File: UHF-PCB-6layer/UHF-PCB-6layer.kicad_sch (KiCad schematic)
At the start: 14 parts, among them IC1 MC100EL1648DG, U1 MAC-24+, U3 TAV1-331+, U4 TPS3103K33DBVR, U5 XMSM0G3507SPT, U6 XC7A100T-CSG324_A

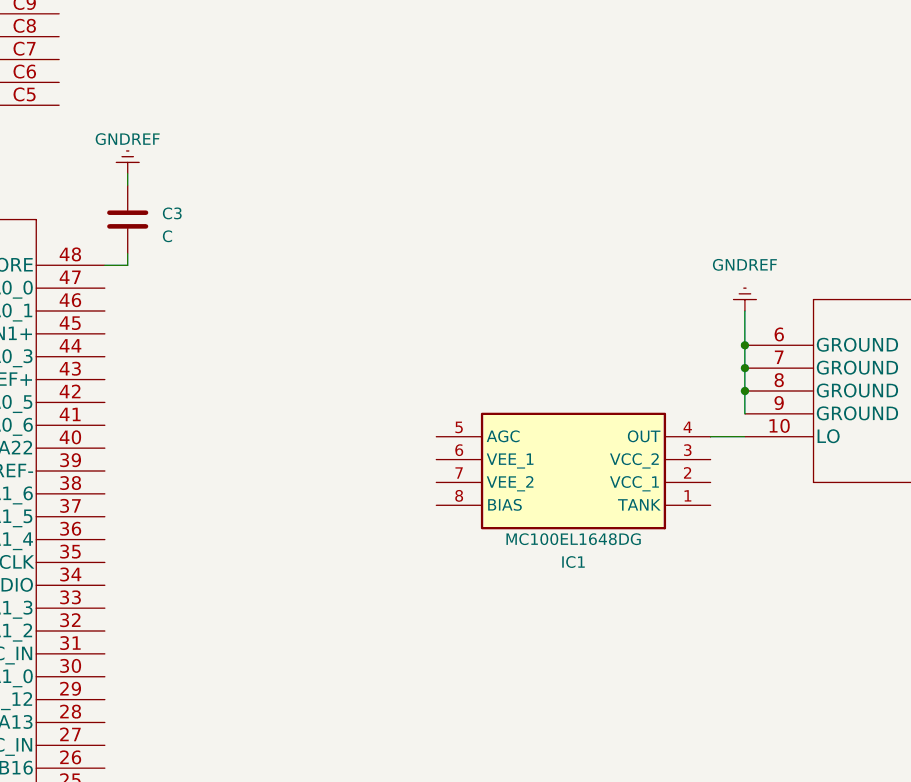
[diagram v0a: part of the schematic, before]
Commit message: added more to VCO circuit
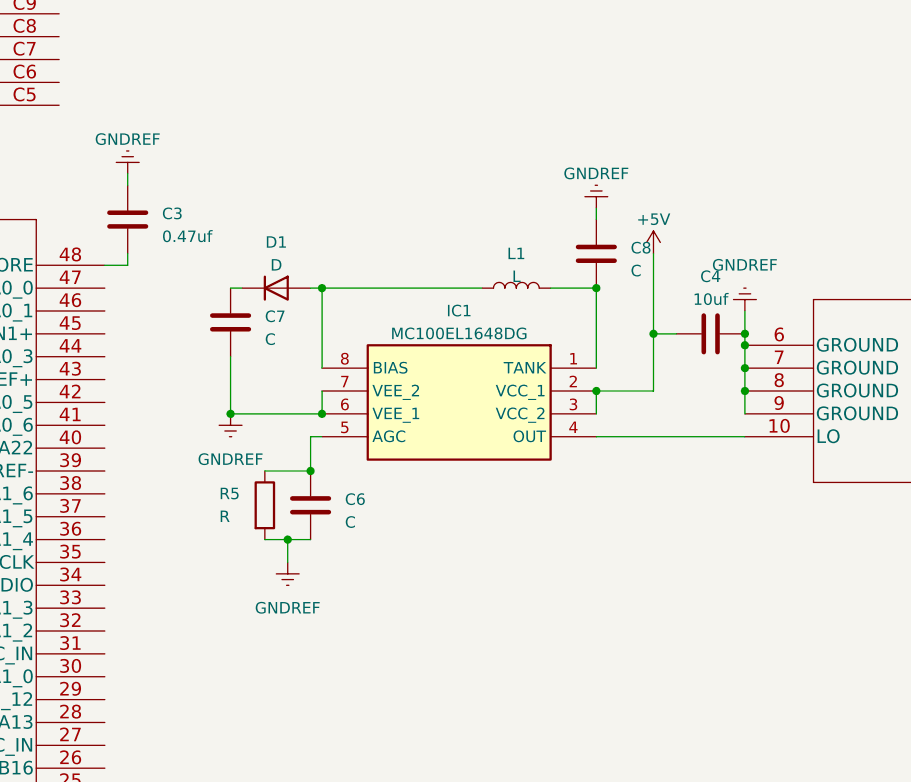
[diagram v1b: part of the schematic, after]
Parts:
- added C4: 10uf, Capacitor_SMD:C_0603_1608Metric, symbol Device:C
- added C6, C7, C8: C, Capacitor_SMD:C_0603_1608Metric, symbol Device:C
- added D1: D, Diode_SMD:D_0603_1608Metric, symbol Device:D
- added L1: L, Inductor_SMD:L_0603_1608Metric, symbol Device:L
- added R5: R, Resistor_SMD:R_0603_1608Metric, symbol Device:R
- C3: value C -> 0.47uf
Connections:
- net +5V: now also IC1.2 (VCC_1), IC1.3 (VCC_2), C4.2
- net GNDREF: now also IC1.6 (VEE_1), IC1.7 (VEE_2), C4.1, C6.1, C7.2, C8.2, R5.2
- net at IC1.1 (TANK): now also C8.1, L1.2
- net at IC1.5 (AGC): now also C6.2, R5.1
- net at IC1.8 (BIAS): now also D1.2 (A), L1.1
- new net: C7.1, D1.1 (K)
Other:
- moved on the sheet: IC1

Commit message: added some gnds
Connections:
- net GNDREF: now also U3.1 (GND)
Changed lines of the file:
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@@
+    (stroke (width 0) (type default))
+  )
+  (wire (pts (xy 373.38 129.54) (xy 373.38 134.62))
     (stroke (width 0) (type default))
   )
@@
         )
       )
+    )
+  )
+  (symbol (lib_id "power:GNDREF") (at 373.38 129.54 180) (unit 1)
+    (in_bom yes) (on_board yes) (dnp no) (fields_autoplaced)
+    (property "Reference" "#PWR013" (at 373.38 123.19 0)
+      (effects (font (size 1.27 1.27)) hide)
+    )
+    (property "Value" "GNDREF" (at 373.38 125.73 0)
+      (effects (font (size 1.27 1.27)))
+    )
+    (property "Footprint" "" (at 373.38 129.54 0)
+      (effects (font (size 1.27 1.27)) hide)
+    )
+    (property "Datasheet" "" (at 373.38 129.54 0)
+      (effects (font (size 1.27 1.27)) hide)
+    )
+    (pin "1")
+    (instances
+      (project "UHF-PCB-6layer"
+        (path "/408f5dbf-8c57-4b84-b0cc-1d788fcf6d08"
+          (reference "#PWR013") (unit 1)
+        )
+      )

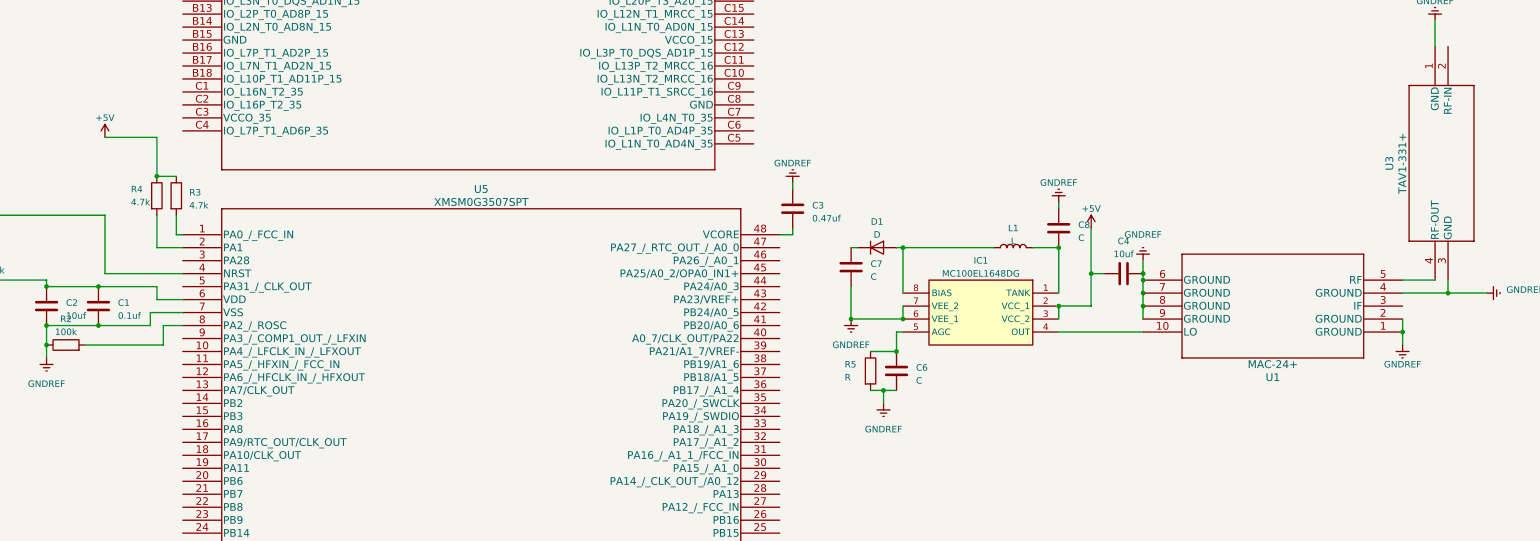
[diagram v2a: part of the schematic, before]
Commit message: added connections between FPGA and micro
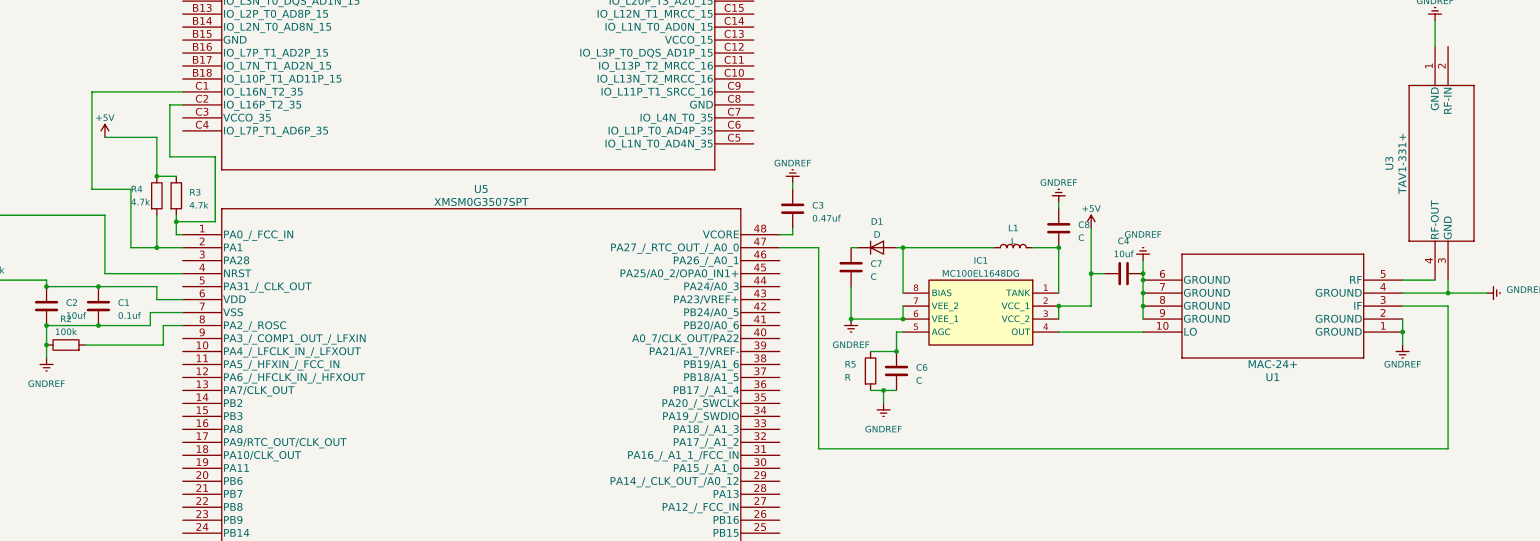
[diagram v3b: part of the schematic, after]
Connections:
- net at U1.3 (IF): now also U5.47 (PA27_/_RTC_OUT_/_A0_0)
- net at R3.2, U5.1 (PA0_/_FCC_IN): now also U6.C2 (IO_L16P_T2_35)
- net at R4.2, U5.2 (PA1): now also U6.C1 (IO_L16N_T2_35)
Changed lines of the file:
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@@
     (rev "MK1")
   )
+  (junction (at 127 168.91) (diameter 0) (color 0 0 0 0)
+  )
   (junction (at 306.07 179.07) (diameter 0) (color 0 0 0 0)
   )
@@
   (junction (at 299.72 185.42) (diameter 0) (color 0 0 0 0)
   )
+  (junction (at 123.19 173.99) (diameter 0) (color 0 0 0 0)
+  )
   (junction (at 123.19 160.02) (diameter 0) (color 0 0 0 0)
   )
@@
     (stroke (width 0) (type default))
   )
+  (wire (pts (xy 375.92 185.42) (xy 367.03 185.42))
+    (stroke (width 0) (type default))
+  )
   (wire (pts (xy 128.27 186.69) (xy 121.92 186.69))
     (stroke (width 0) (type default))
@@
     (stroke (width 0) (type default))
   )
+  (wire (pts (xy 128.27 143.51) (xy 110.49 143.51))
+    (stroke (width 0) (type default))
+  )
   (wire (pts (xy 306.07 170.18) (xy 306.07 179.07))
     (stroke (width 0) (type default))
@@
     (stroke (width 0) (type default))
   )
+  (wire (pts (xy 127 168.91) (xy 127 167.64))
+    (stroke (width 0) (type default))
+  )
   (wire (pts (xy 316.23 182.88) (xy 316.23 180.34))
     (stroke (width 0) (type default))
   )
+  (wire (pts (xy 252.73 213.36) (xy 375.92 213.36))
+    (stroke (width 0) (type default))
+  )
   (wire (pts (xy 375.92 182.88) (xy 367.03 182.88))
     (stroke (width 0) (type default))
   )
+  (wire (pts (xy 125.73 156.21) (xy 134.62 156.21))
+    (stroke (width 0) (type default))
+  )
   (wire (pts (xy 121.92 189.23) (xy 111.76 189.23))
     (stroke (width 0) (type default))
@@
     (stroke (width 0) (type default))
   )
+  (wire (pts (xy 110.49 143.51) (xy 110.49 162.56))
+    (stroke (width 0) (type default))
+  )
   (wire (pts (xy 316.23 185.42) (xy 316.23 182.88))
     (stroke (width 0) (type default))
@@
     (stroke (width 0) (type default))
   )
-  (wire (pts (xy 127 171.45) (xy 127 167.64))
+  (wire (pts (xy 127 171.45) (xy 127 168.91))
     (stroke (width 0) (type default))
   )
@@
     (stroke (width 0) (type default))
   )
+  (wire (pts (xy 110.49 162.56) (xy 118.11 162.56))
+    (stroke (width 0) (type default))
+  )
   (wire (pts (xy 247.65 171.45) (xy 245.11 171.45))
     (stroke (width 0) (type default))
@@
     (stroke (width 0) (type default))
   )
+  (wire (pts (xy 134.62 168.91) (xy 127 168.91))
+    (stroke (width 0) (type default))
+  )
   (wire (pts (xy 316.23 180.34) (xy 316.23 179.07))
     (stroke (width 0) (type default))
@@
     (stroke (width 0) (type default))
   )
+  (wire (pts (xy 128.27 146.05) (xy 125.73 146.05))
+    (stroke (width 0) (type default))
+  )
   (wire (pts (xy 247.65 161.29) (xy 247.65 162.56))
     (stroke (width 0) (type default))
@@
     (stroke (width 0) (type default))
   )
+  (wire (pts (xy 252.73 173.99) (xy 252.73 213.36))
+    (stroke (width 0) (type default))
+  )
   (wire (pts (xy 267.97 190.5) (xy 267.97 194.31))
     (stroke (width 0) (type default))
@@
     (stroke (width 0) (type default))
   )
+  (wire (pts (xy 118.11 173.99) (xy 123.19 173.99))
+    (stroke (width 0) (type default))
+  )
   (wire (pts (xy 259.08 181.61) (xy 259.08 187.96))
     (stroke (width 0) (type default))
@@
     (stroke (width 0) (type default))
   )
+  (wire (pts (xy 134.62 156.21) (xy 134.62 168.91))
+    (stroke (width 0) (type default))
+  )
   (wire (pts (xy 123.19 173.99) (xy 123.19 167.64))
     (stroke (width 0) (type default))
   )
+  (wire (pts (xy 118.11 162.56) (xy 118.11 173.99))
+    (stroke (width 0) (type default))
+  )
   (wire (pts (xy 128.27 189.23) (xy 124.46 189.23))
     (stroke (width 0) (type default))
@@
     (stroke (width 0) (type default))
   )
+  (wire (pts (xy 375.92 213.36) (xy 375.92 185.42))
+    (stroke (width 0) (type default))
+  )
   (wire (pts (xy 265.43 201.93) (xy 265.43 204.47))
     (stroke (width 0) (type default))
@@
     (stroke (width 0) (type default))
   )
+  (wire (pts (xy 245.11 173.99) (xy 252.73 173.99))
+    (stroke (width 0) (type default))
+  )
   (wire (pts (xy 294.64 173.99) (xy 299.72 173.99))
     (stroke (width 0) (type default))
@@
     (stroke (width 0) (type default))
   )
+  (wire (pts (xy 125.73 146.05) (xy 125.73 156.21))
+    (stroke (width 0) (type default))
+  )

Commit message: maybe some edits idk
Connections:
- net at R3.2, U5.1 (PA0_/_FCC_IN): no longer U6.C2 (IO_L16P_T2_35)
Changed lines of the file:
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@@
     (rev "MK1")
   )
-  (junction (at 127 168.91) (diameter 0) (color 0 0 0 0)
-  )
   (junction (at 306.07 179.07) (diameter 0) (color 0 0 0 0)
   )
@@
     (stroke (width 0) (type default))
   )
-  (wire (pts (xy 127 168.91) (xy 127 167.64))
-    (stroke (width 0) (type default))
-  )
   (wire (pts (xy 316.23 182.88) (xy 316.23 180.34))
     (stroke (width 0) (type default))
@@
     (stroke (width 0) (type default))
   )
-  (wire (pts (xy 125.73 156.21) (xy 134.62 156.21))
-    (stroke (width 0) (type default))
-  )
   (wire (pts (xy 121.92 189.23) (xy 111.76 189.23))
     (stroke (width 0) (type default))
@@
     (stroke (width 0) (type default))
   )
-  (wire (pts (xy 127 171.45) (xy 127 168.91))
+  (wire (pts (xy 127 171.45) (xy 127 167.64))
     (stroke (width 0) (type default))
   )
@@
     (stroke (width 0) (type default))
   )
-  (wire (pts (xy 134.62 168.91) (xy 127 168.91))
-    (stroke (width 0) (type default))
-  )
   (wire (pts (xy 316.23 180.34) (xy 316.23 179.07))
     (stroke (width 0) (type default))
@@
     (stroke (width 0) (type default))
   )
-  (wire (pts (xy 128.27 146.05) (xy 125.73 146.05))
-    (stroke (width 0) (type default))
-  )
   (wire (pts (xy 247.65 161.29) (xy 247.65 162.56))
     (stroke (width 0) (type default))
@@
     (stroke (width 0) (type default))
   )
-  (wire (pts (xy 134.62 156.21) (xy 134.62 168.91))
-    (stroke (width 0) (type default))
-  )
   (wire (pts (xy 123.19 173.99) (xy 123.19 167.64))
     (stroke (width 0) (type default))
@@
     (stroke (width 0) (type default))
   )
-  (wire (pts (xy 125.73 146.05) (xy 125.73 156.21))
-    (stroke (width 0) (type default))
-  )

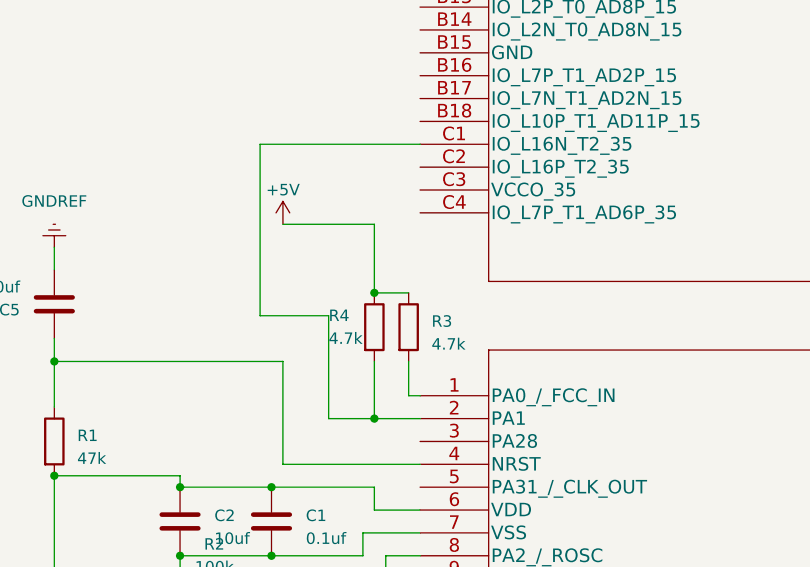
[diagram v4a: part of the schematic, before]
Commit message: added wire to schematic
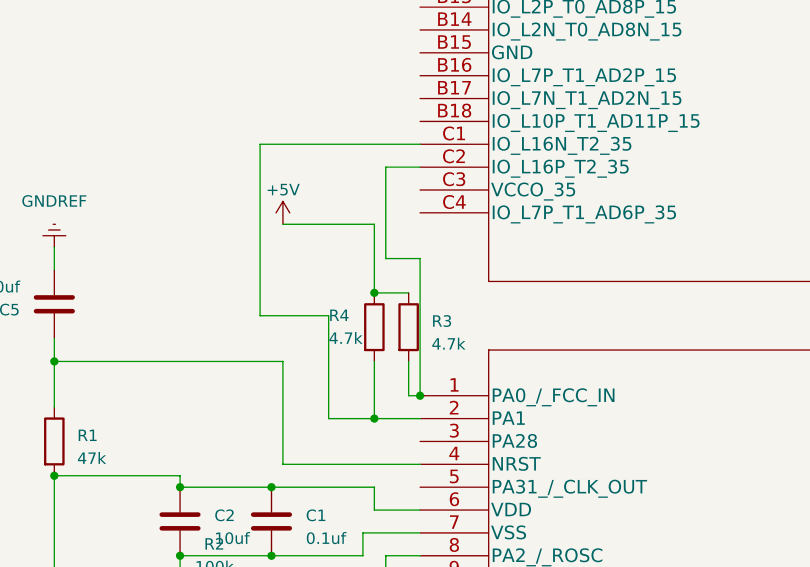
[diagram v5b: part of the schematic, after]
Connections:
- net at R3.2, U5.1 (PA0_/_FCC_IN): now also U6.C2 (IO_L16P_T2_35)
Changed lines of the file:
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@@
   (junction (at 316.23 182.88) (diameter 0) (color 0 0 0 0)
   )
+  (junction (at 128.27 171.45) (diameter 0) (color 0 0 0 0)
+  )
   (junction (at 316.23 185.42) (diameter 0) (color 0 0 0 0)
   )
@@
     (stroke (width 0) (type default))
   )
+  (wire (pts (xy 128.27 156.21) (xy 124.46 156.21))
+    (stroke (width 0) (type default))
+  )
   (wire (pts (xy 110.49 143.51) (xy 110.49 162.56))
     (stroke (width 0) (type default))
@@
     (stroke (width 0) (type default))
   )
+  (wire (pts (xy 128.27 171.45) (xy 128.27 156.21))
+    (stroke (width 0) (type default))
+  )
   (wire (pts (xy 123.19 160.02) (xy 127 160.02))
     (stroke (width 0) (type default))
@@
     (stroke (width 0) (type default))
   )
+  (wire (pts (xy 124.46 146.05) (xy 128.27 146.05))
+    (stroke (width 0) (type default))
+  )
   (wire (pts (xy 123.19 173.99) (xy 123.19 167.64))
     (stroke (width 0) (type default))
@@
     (stroke (width 0) (type default))
   )
+  (wire (pts (xy 124.46 156.21) (xy 124.46 146.05))
+    (stroke (width 0) (type default))
+  )

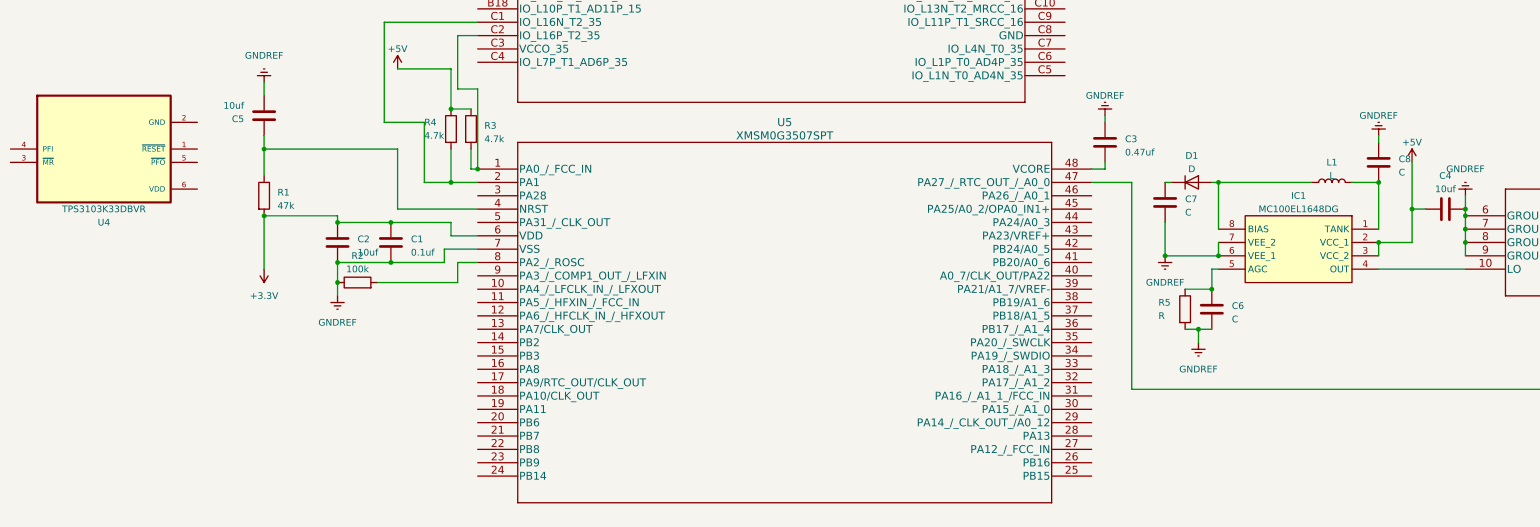
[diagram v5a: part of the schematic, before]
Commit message: added 2.3MHz LPF
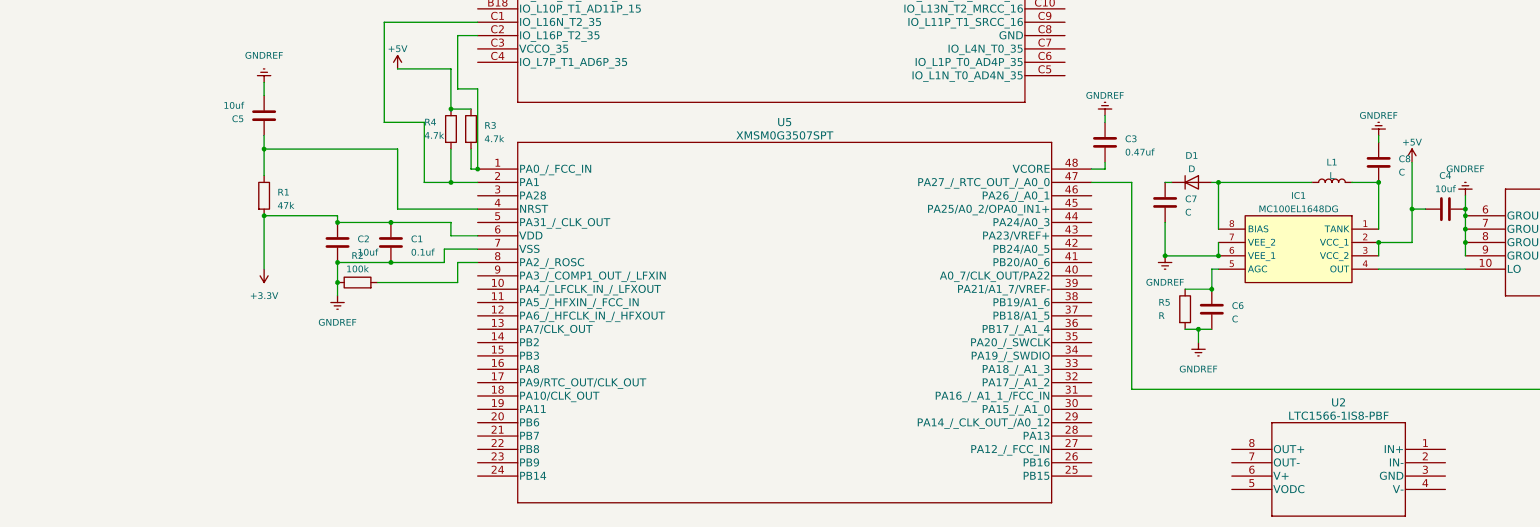
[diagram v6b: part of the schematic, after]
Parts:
- removed U4: TPS3103K33DBVR, SOT95P280X145-6N, symbol TPS3103K33DBVR:TPS3103K33DBVR
- added U2: LTC1566-1IS8-PBF, SO-8_S_LIT, symbol FilterLOW:LTC1566-1IS8-PBF
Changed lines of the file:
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@@
+    )
+  )
+  (symbol (lib_id "FilterLOW:LTC1566-1IS8-PBF") (at 312.42 224.79 0) (mirror y) (unit 1)
+    (in_bom yes) (on_board yes) (dnp no)
+    (property "Reference" "U2" (at 292.1 215.9 0)
+      (effects (font (size 1.524 1.524)))
+    )
+    (property "Value" "LTC1566-1IS8-PBF" (at 292.1 218.44 0)
+      (effects (font (size 1.524 1.524)))
+    )
+    (property "Footprint" "SO-8_S_LIT" (at 292.1 218.694 0)
+      (effects (font (size 1.524 1.524)) hide)
+    )
+    (property "Datasheet" "" (at 312.42 224.79 0)
+      (effects (font (size 1.524 1.524)))
+    )
+    (pin "1")
+    (pin "2")
+    (pin "3")
+    (pin "4")
+    (pin "5")
+    (pin "6")
+    (pin "7")
+    (pin "8")
+    (instances
+      (project "UHF-PCB-6layer"
+        (path "/408f5dbf-8c57-4b84-b0cc-1d788fcf6d08"
+          (reference "U2") (unit 1)
+        )
+      )
     )
   )
@@
         )
       )
-    )
-  )
-  (symbol (lib_id "TPS3103K33DBVR:TPS3103K33DBVR") (at 57.15 167.64 0) (mirror x) (unit 1)
-    (in_bom yes) (on_board yes) (dnp no)
-    (property "Reference" "U4" (at 57.15 181.61 0)
-      (effects (font (size 1.27 1.27)))
-    )
-    (property "Value" "TPS3103K33DBVR" (at 57.15 179.07 0)
-      (effects (font (size 1.27 1.27)))
-    )
-    (property "Footprint" "SOT95P280X145-6N" (at 57.15 167.64 0)
-      (effects (font (size 1.27 1.27)) (justify left bottom) hide)
-    )
-    (property "Datasheet" "" (at 57.15 167.64 0)
-      (effects (font (size 1.27 1.27)) (justify left bottom) hide)
-    )
-    (pin "1")
-    (pin "2")
-    (pin "3")
-    (pin "4")
-    (pin "5")
-    (pin "6")
-    (instances
-      (project "UHF-PCB-6layer"
-        (path "/408f5dbf-8c57-4b84-b0cc-1d788fcf6d08"
-          (reference "U4") (unit 1)
-        )
-      )
